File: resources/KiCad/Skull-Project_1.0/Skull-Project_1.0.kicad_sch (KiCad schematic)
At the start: 6 parts, among them SW1 SW_SPST, SW2 SW_SPST

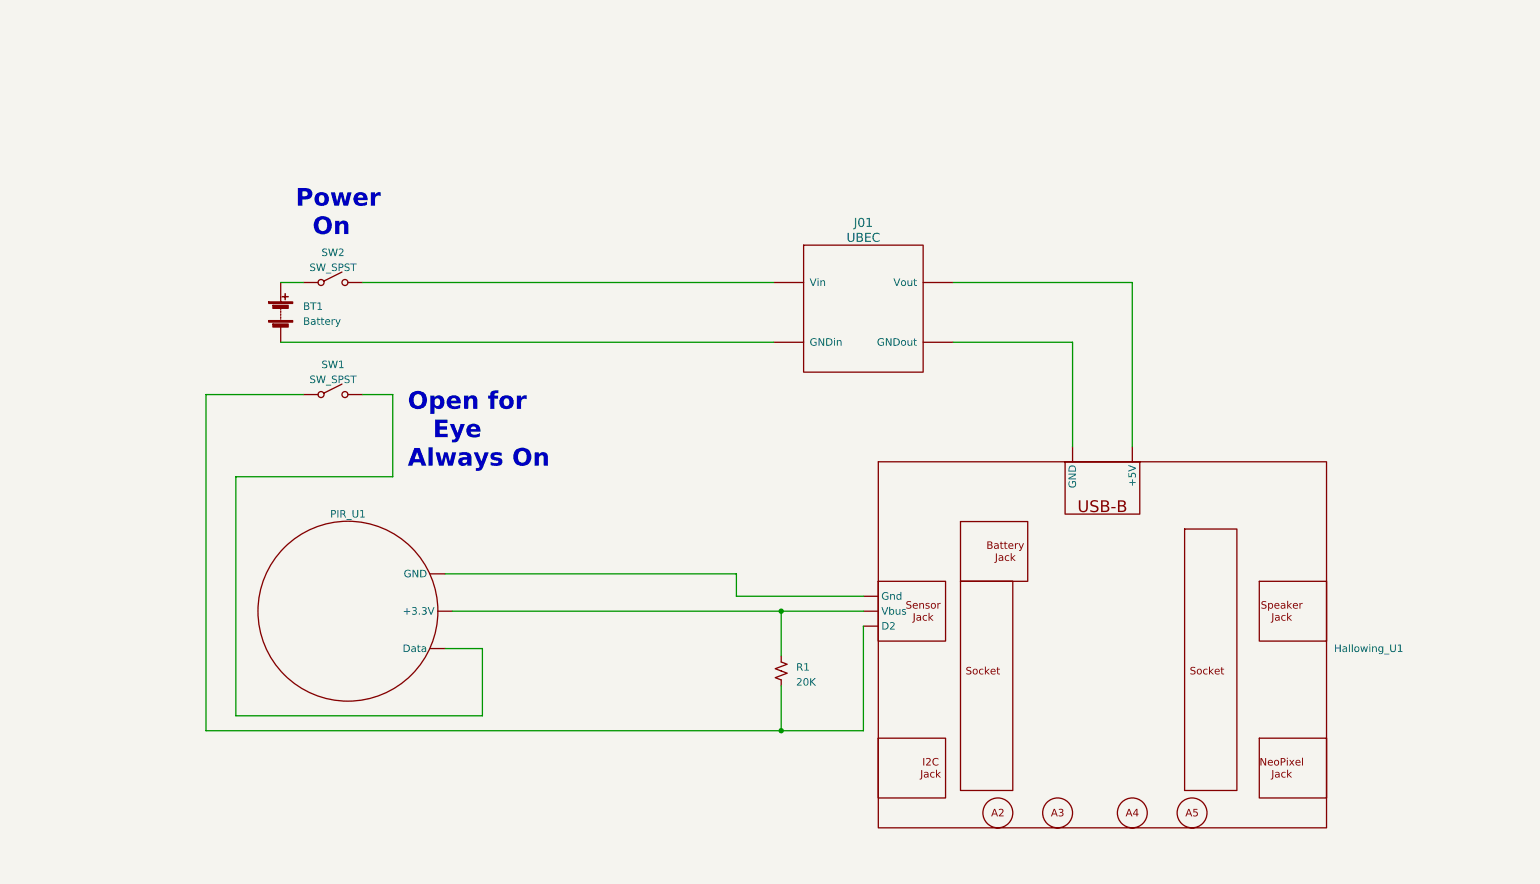
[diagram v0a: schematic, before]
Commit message: update schematic
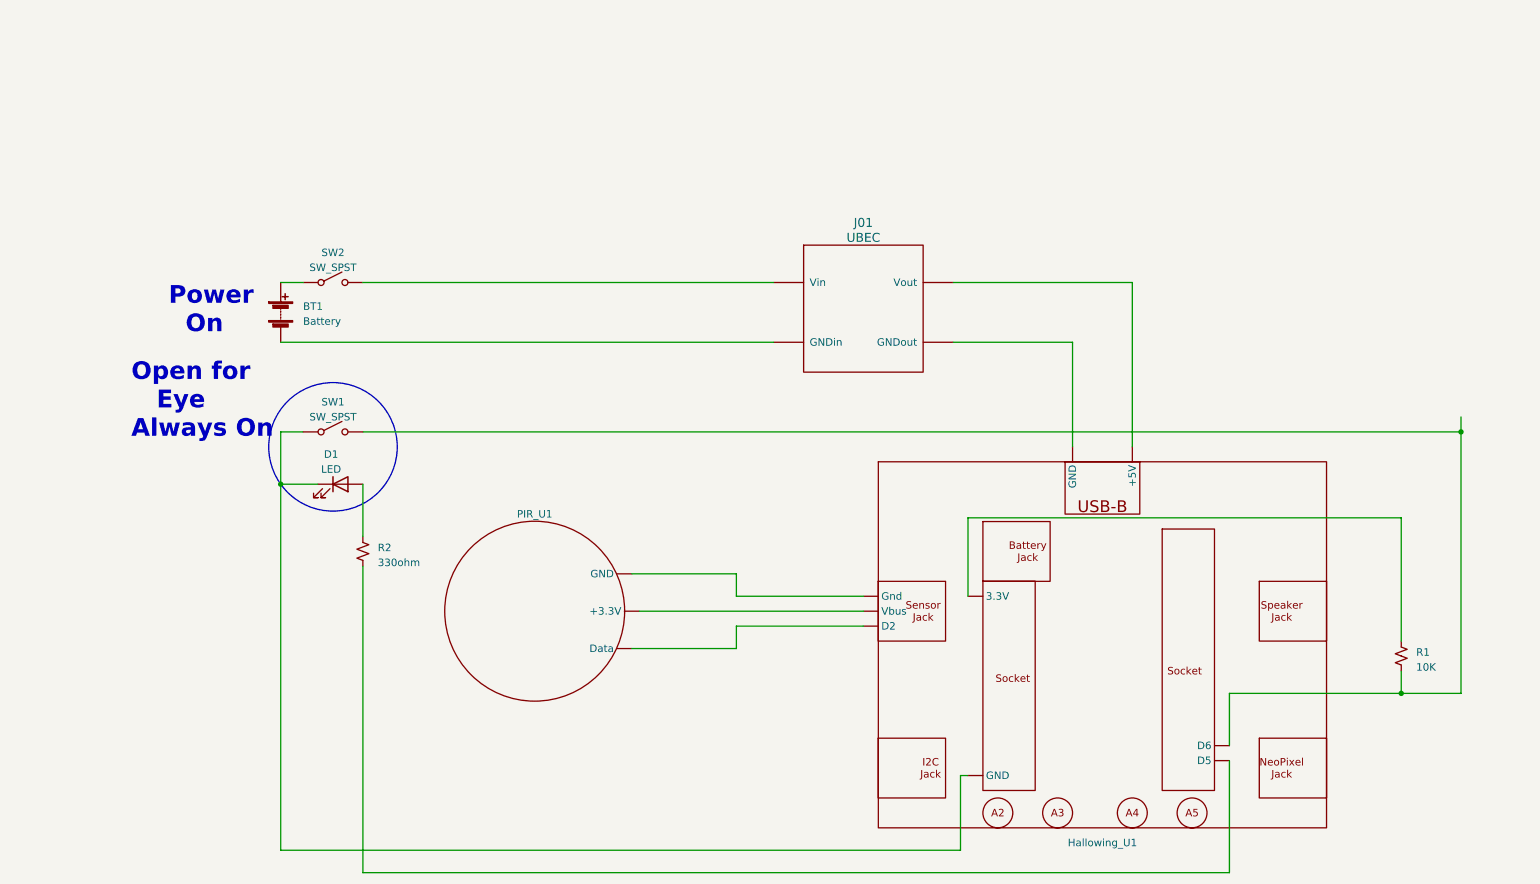
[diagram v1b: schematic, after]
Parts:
- added D1: LED, symbol Device:LED
- added R2: 330ohm, symbol Device:R_Small_US
- R1: value 20K -> 10K
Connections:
- net at SW2.~ (B): now also BT1.1 (+)
- net at Hallowing_U1. (Vbus), PIR_U1. (GND): no longer R1.1
- net at SW1.~ (B): now also Hallowing_U1. (Vbus), D1.1 (K); no longer PIR_U1. (GND)
- new net: D1.2 (A), R2.1
- new net: Hallowing_U1. (Vbus), R2.2
- new net: Hallowing_U1. (Vbus), R1.1
- new net: Hallowing_U1. (Vbus), R1.2, SW1.~ (B)
- new net: Hallowing_U1. (Vbus), PIR_U1. (GND) (x2)
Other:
- moved on the sheet: PIR_U1, R1, SW1

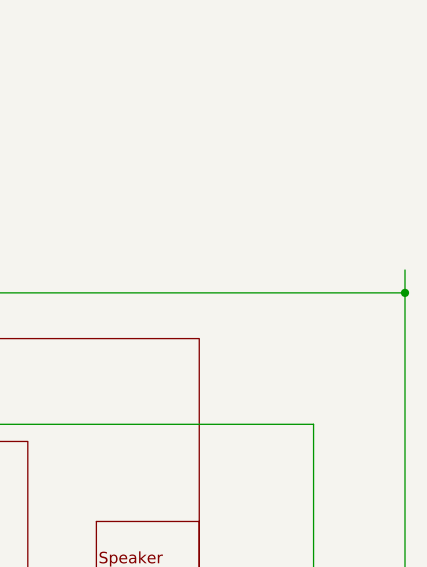
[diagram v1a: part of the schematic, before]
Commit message: update schematic
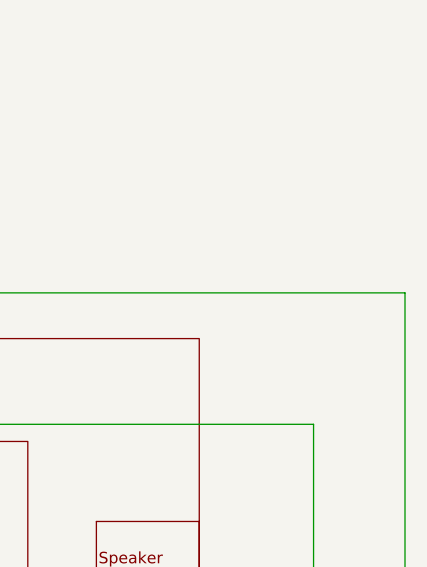
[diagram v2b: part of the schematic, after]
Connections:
- net at SW2.~ (B): now also BT1.1 (+)
- net at Hallowing_U1. (Vbus): now also PIR_U1. (GND)
- new net: Hallowing_U1. (Vbus), R1.2, SW1.~ (B)
- new net: Hallowing_U1. (Vbus), PIR_U1. (GND) (x2)
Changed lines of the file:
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@@
     (rev "1.0")
     (company "github.com/Mark-MDO47/Skull-Project")
+    (comment 1 "NOTE: Hallowing as from back (not display)")
   )
   (junction (at 63.5 96.52) (diameter 0) (color 0 0 0 0)
   )
   (junction (at 254 132.08) (diameter 0) (color 0 0 0 0)
-  )
-  (junction (at 264.16 87.63) (diameter 0) (color 0 0 0 0)
   )
   (wire (pts (xy 63.5 72.39) (xy 147.32 72.39))
@@
     (stroke (width 0) (type default))
   )
-  (wire (pts (xy 264.16 85.09) (xy 264.16 87.63))
-    (stroke (width 0) (type default))
-  )

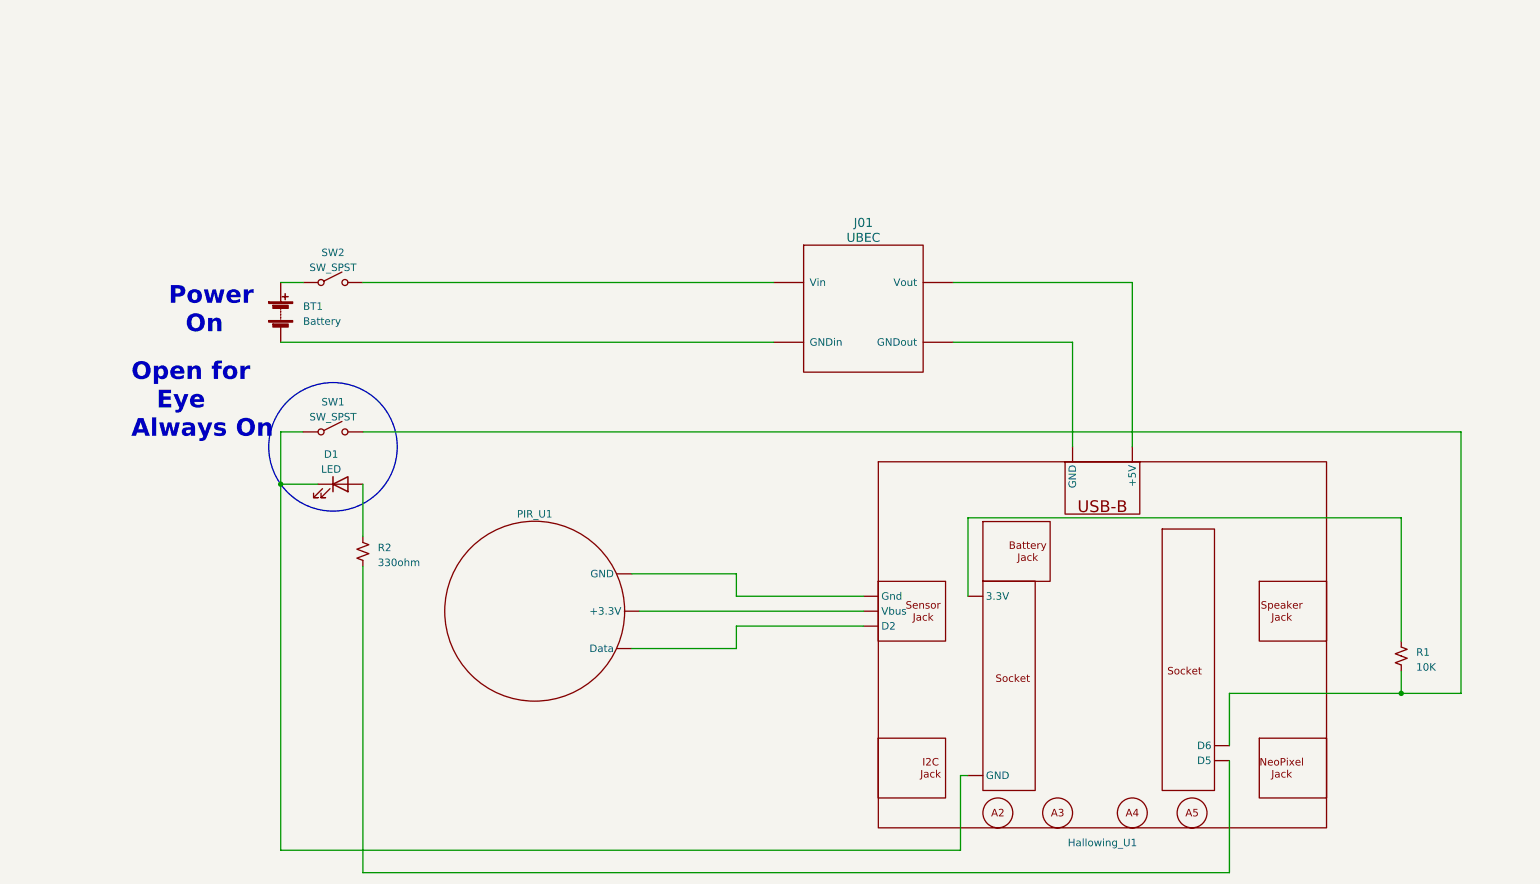
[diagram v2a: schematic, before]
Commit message: Update schematic for toggle push-button with LED
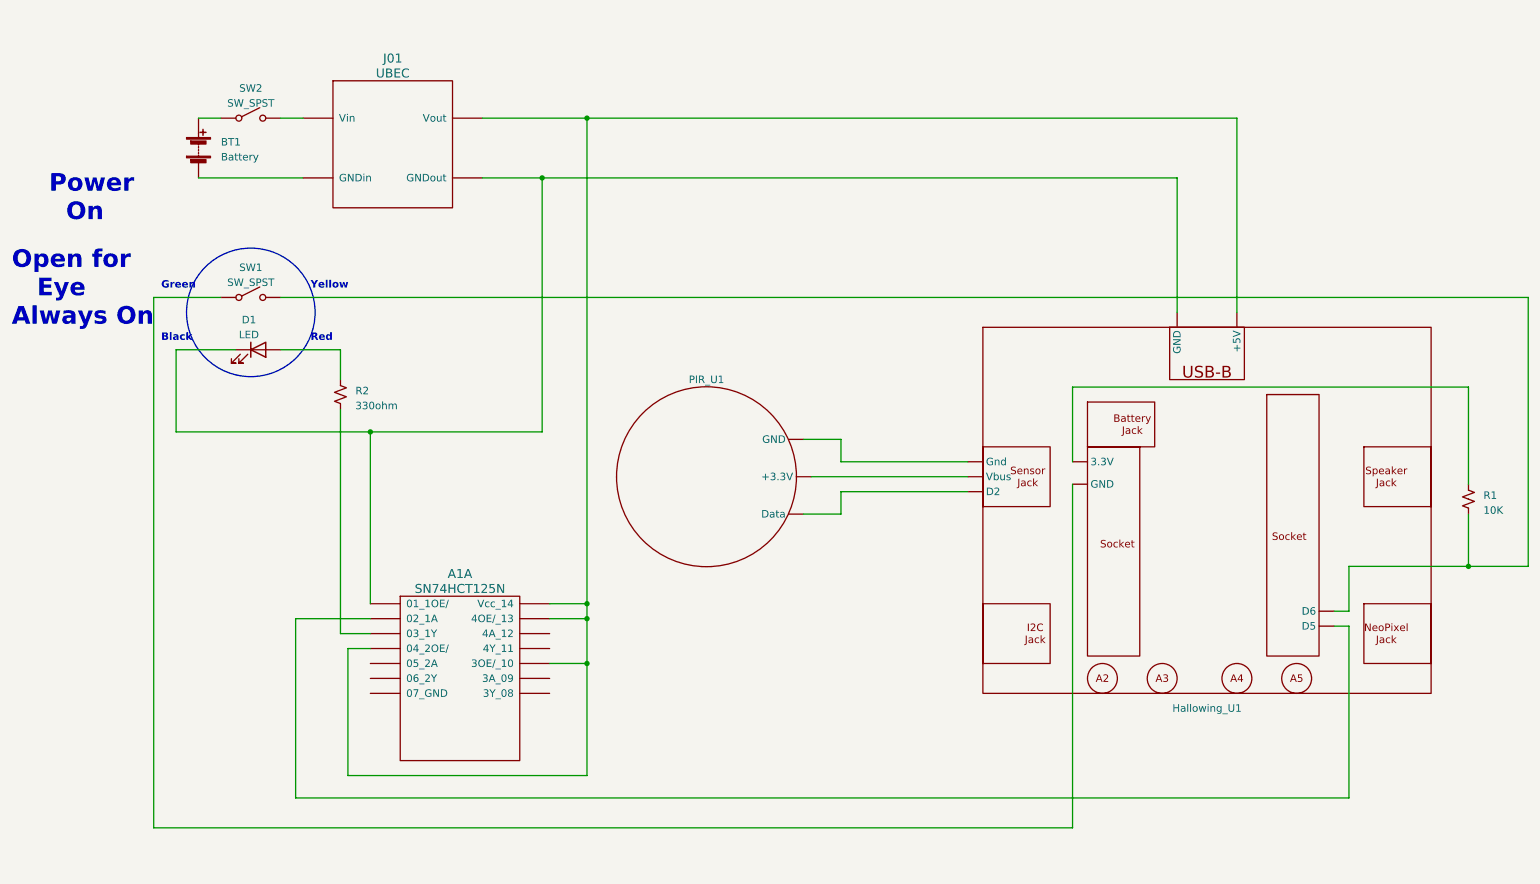
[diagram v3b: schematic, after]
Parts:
- added A1: SN74HCT125N, symbol MDO:SN74HCT125N
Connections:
- net at Hallowing_U1. (Vbus): now also PIR_U1. (GND); no longer R2.2
- net at SW2.~ (B): now also BT1.1 (+)
- new net: A1.~ (Vcc_14), Hallowing_U1. (Vbus) (x2)
- new net: A1.~ (Vcc_14), D1.1 (K), Hallowing_U1. (Vbus)
- new net: Hallowing_U1. (Vbus), R1.2, SW1.~ (B)
- new net: Hallowing_U1. (Vbus), SW1.~ (B)
- new net: Hallowing_U1. (Vbus), PIR_U1. (GND) (x2)
- new net: A1.~ (Vcc_14), R2.2
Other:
- note added: "Black"
- note added: "Green"
- note added: "Red"
- note added: "Yellow"
- moved on the sheet: BT1, D1, PIR_U1, R1, R2, SW1, SW2

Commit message: 3.3V lights switch LED; much simpler
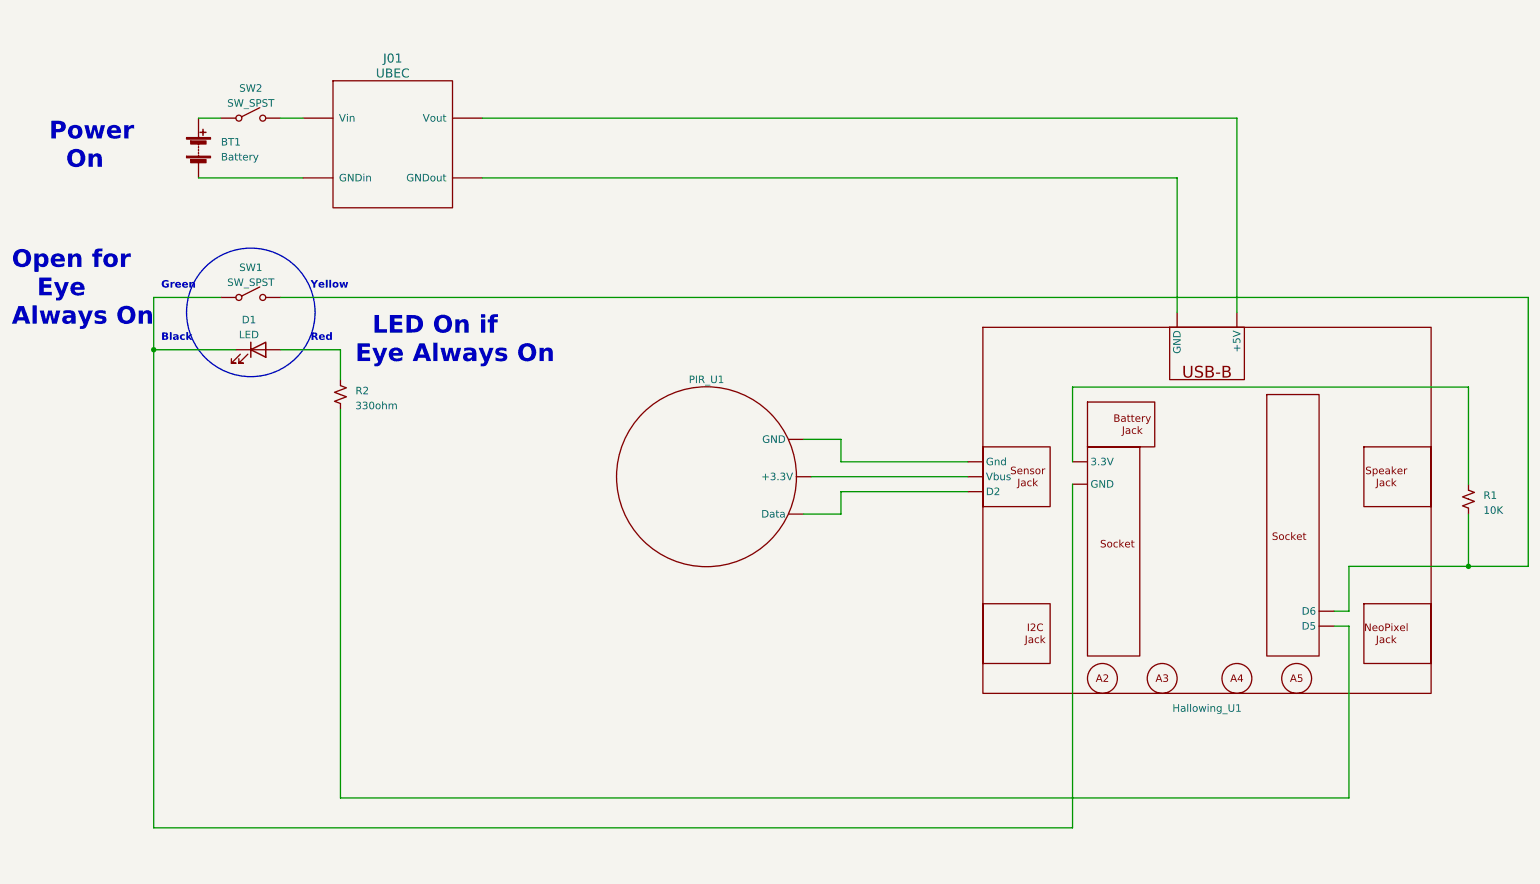
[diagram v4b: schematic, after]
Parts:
- removed A1: SN74HCT125N, symbol MDO:SN74HCT125N
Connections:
- net at Hallowing_U1. (Vbus): now also PIR_U1. (GND)
- net at D1.1 (K), Hallowing_U1. (Vbus): now also SW1.~ (B)
- net at R2.2: now also Hallowing_U1. (Vbus)
- net at SW2.~ (B): now also BT1.1 (+)
- new net: Hallowing_U1. (Vbus), R1.2, SW1.~ (B)
- new net: Hallowing_U1. (Vbus), PIR_U1. (GND) (x2)
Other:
- note added: "LED On if Eye Always On"

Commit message: update schematic
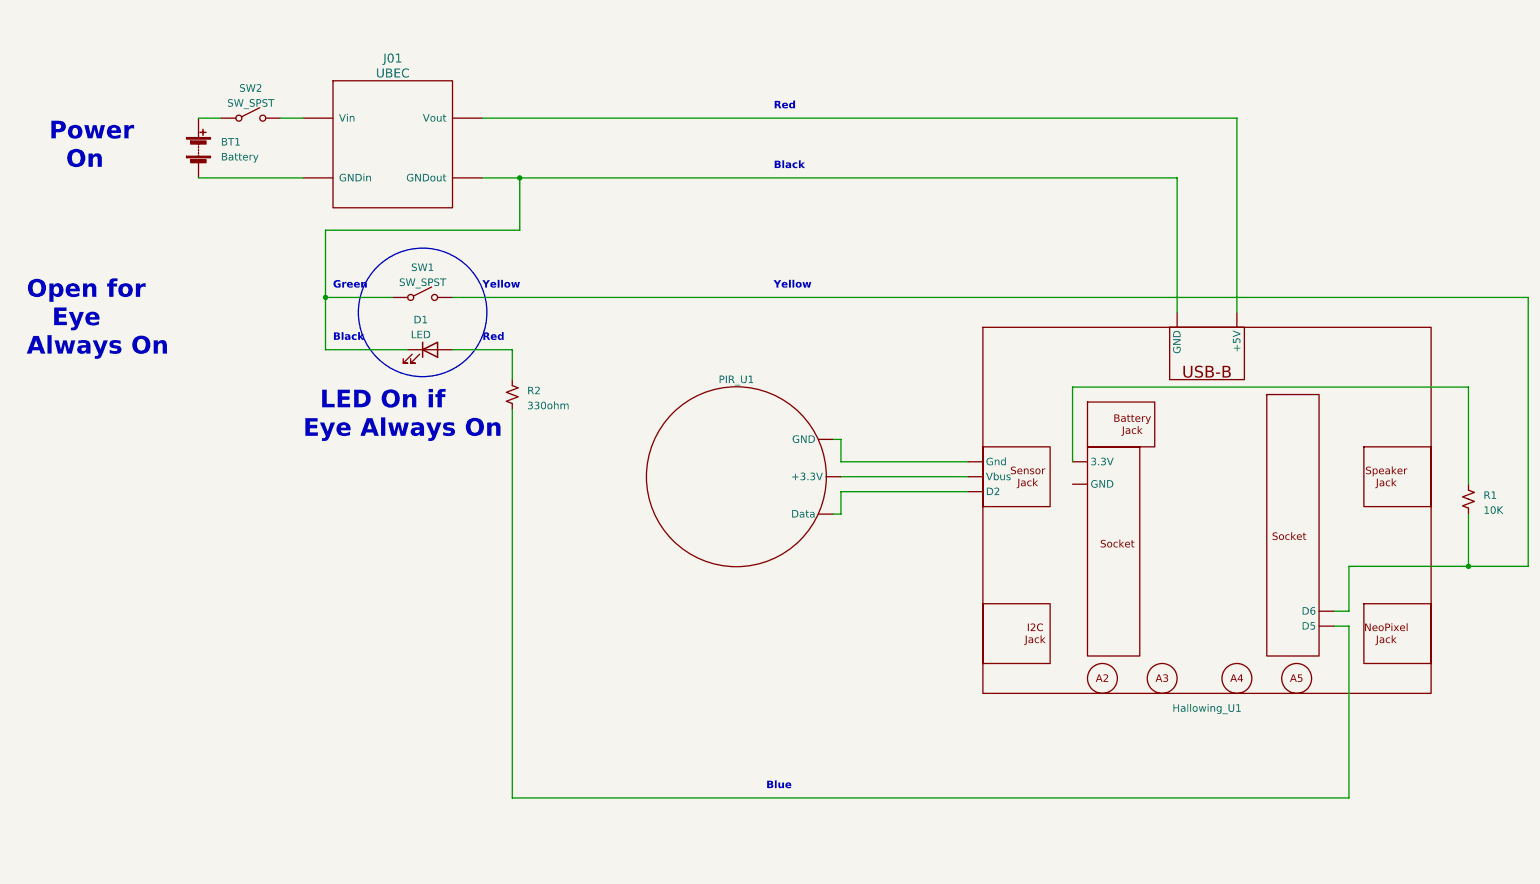
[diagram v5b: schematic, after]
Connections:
- net at Hallowing_U1. (Vbus): now also PIR_U1. (GND)
- net at SW2.~ (B): now also BT1.1 (+)
- new net: Hallowing_U1. (Vbus), R1.2, SW1.~ (B)
- new net: Hallowing_U1. (Vbus), PIR_U1. (GND) (x2)
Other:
- note added: "Blue"
- moved on the sheet: D1, PIR_U1, R2, SW1
